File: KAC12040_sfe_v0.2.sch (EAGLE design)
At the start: 9 parts

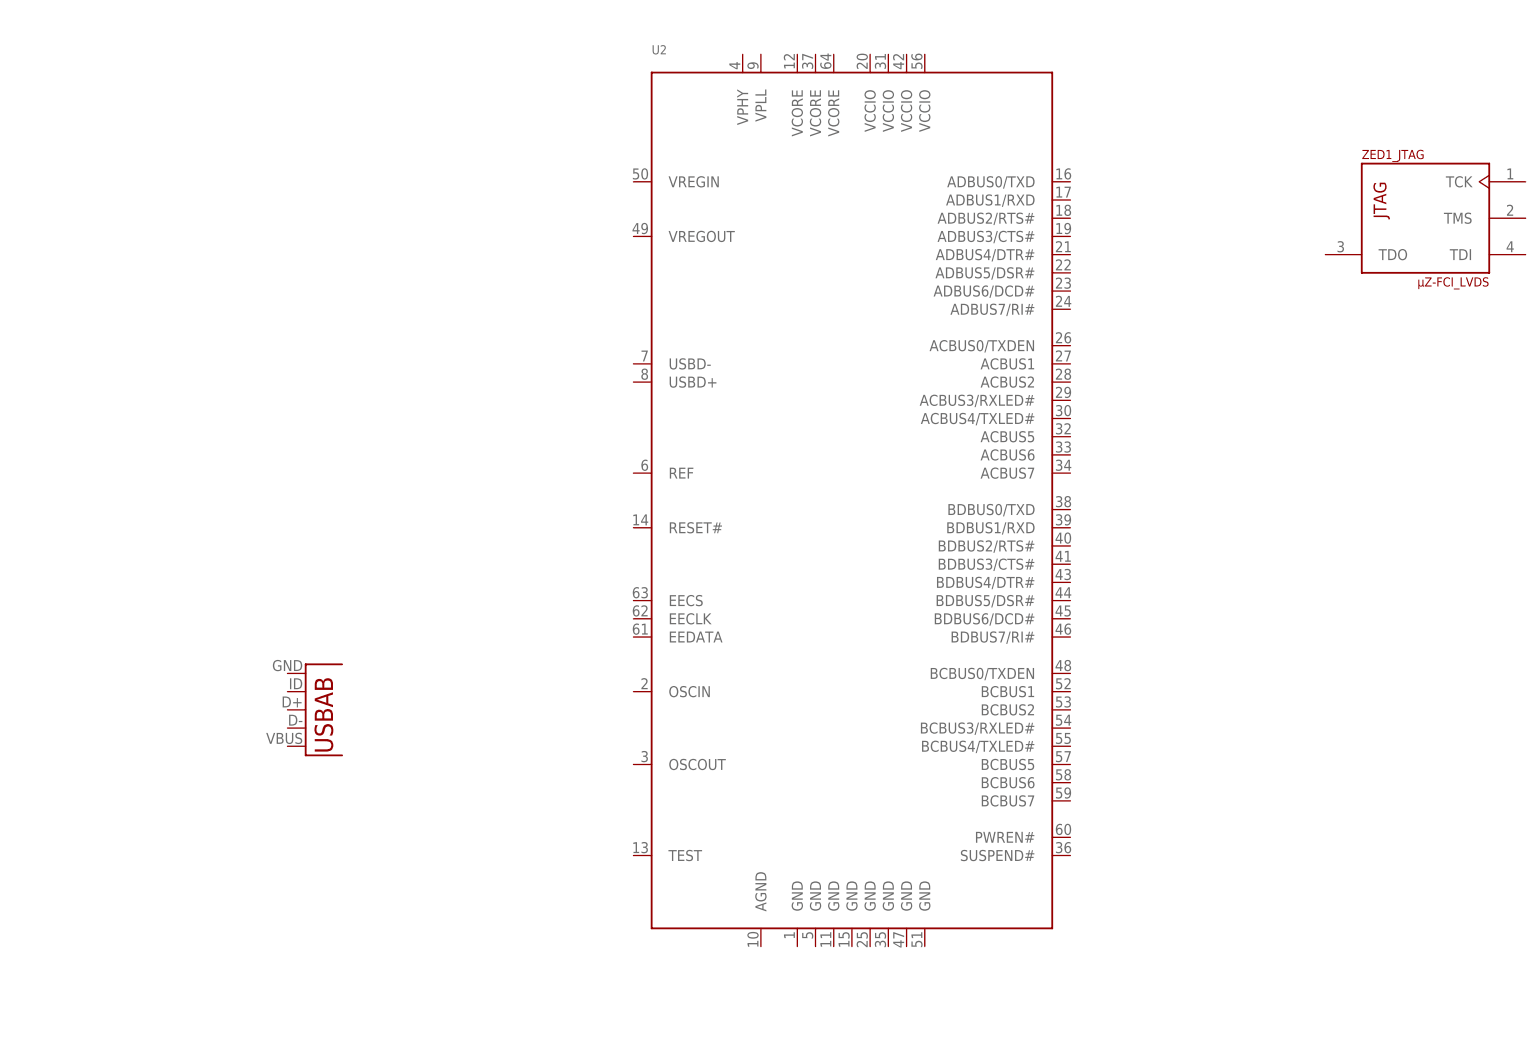
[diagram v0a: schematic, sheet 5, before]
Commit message: Minor library changes and part placement
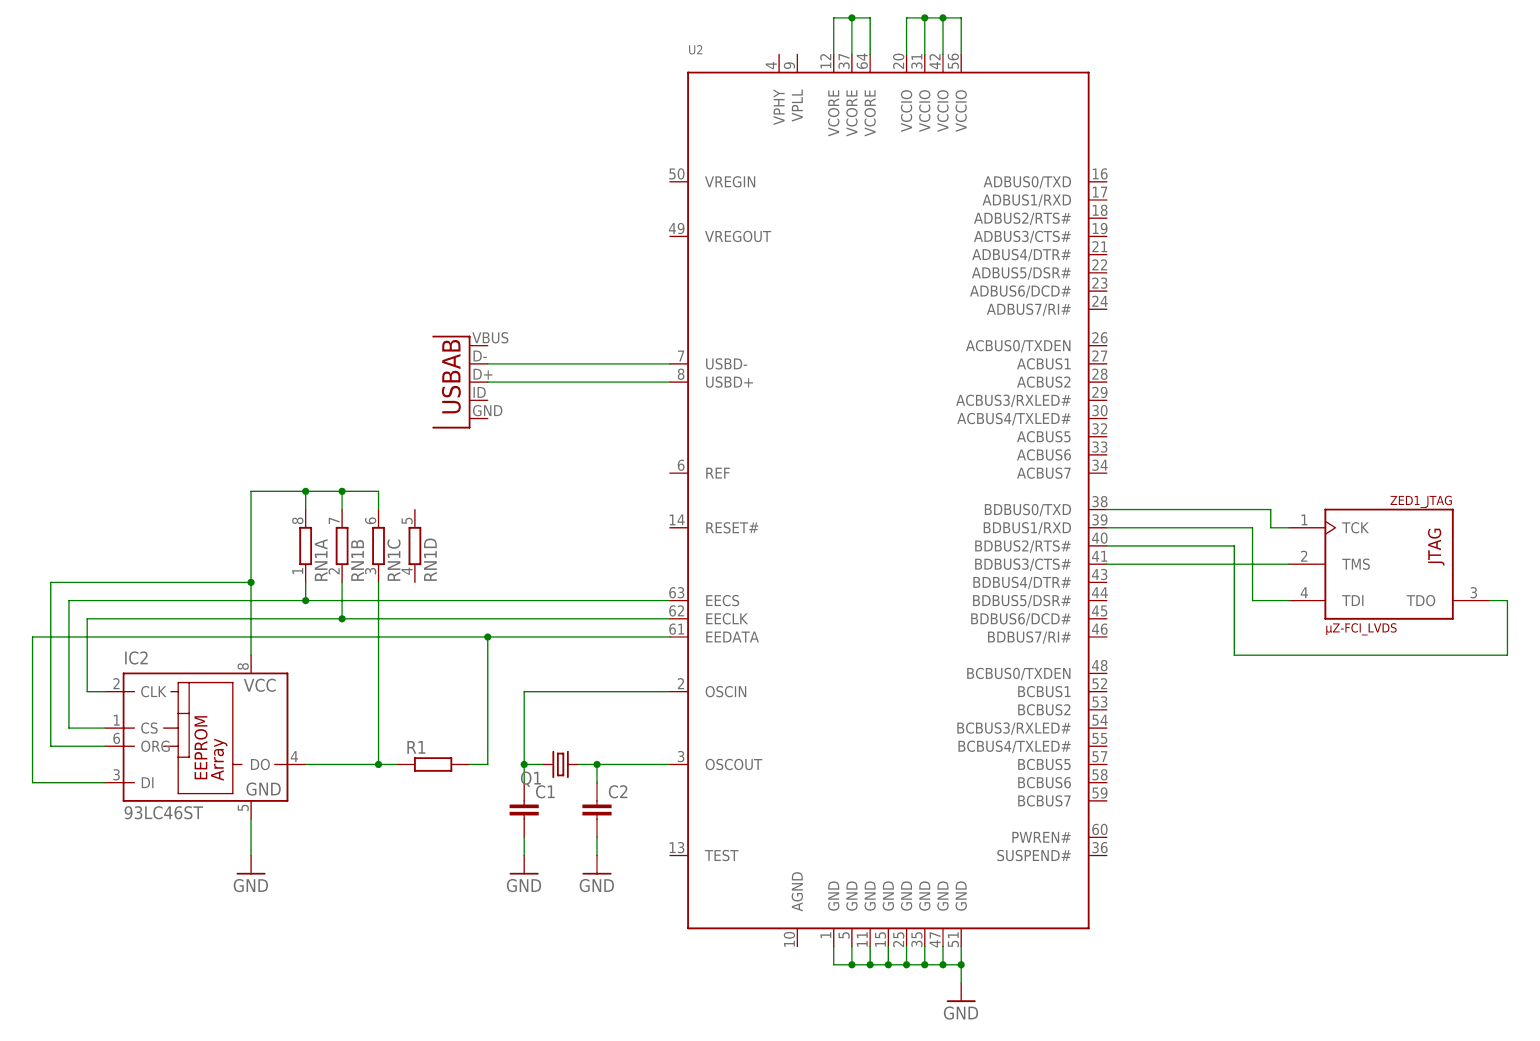
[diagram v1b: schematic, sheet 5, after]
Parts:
- removed U$2: MICRO-SD3, micro-sd:MICRO-SD3
- added C1, C2: (no value), rcl:C-EUC0402K
- added IC2: 93LC46ST, microchip:93LC46ST
- added Q1: (no value), crystal:CRYSTALCTS406
- added R1: (no value), rcl:R-EU_R0402
- added RN1: (no value), resistor-dil:4R-N0402ARV341
- added U$5: ADV7513, adv7513:ADV7513
- added µSD0: MICRO-SD3, micro-sd:MICRO-SD3
- U$1: value KAC-12040 -> KAC-12040-RB501T4; device KAC-12040:KAC-12040 -> KAC-12040:KAC-12040-RB501T4
- renumbered U$3 to µSD1
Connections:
- new net B0_CLK: U$4.B0_CLK, µSD0.5
- new net B0_CMD: U$4.B0_CMD, µSD0.3
- new net B0_DAT0: U$4.B0_DAT0, µSD0.7
- new net B0_DAT1: U$4.B0_DAT1, µSD0.8
- new net B0_DAT2: U$4.B0_DAT2, µSD0.1
- new net B0_DAT3: U$4.B0_DAT3, µSD0.2
- new net B1_CLK: U$4.B1_CLK, µSD1.5
- new net B1_CMD: U$4.B1_CMD, µSD1.3
- new net B1_DAT0: U$4.B1_DAT0, µSD1.7
- new net B1_DAT1: U$4.B1_DAT1, µSD1.8
- new net B1_DAT2: U$4.B1_DAT2, µSD1.1
- new net B1_DAT3: U$4.B1_DAT3, µSD1.2
- new net EE_CLK: IC2.CLK, RN1B.1, U2.EECLK
- new net EE_CS: IC2.CS, RN1A.1, U2.EECS
- new net EE_DATA: IC2.DI, R1.2, U2.EEDATA
- new net GND: C1.2, C2.2, IC2.GND, U2.GND@1, U2.GND@2, U2.GND@3, U2.GND@4, U2.GND@5, U2.GND@6, U2.GND@7, U2.GND@8
- new net N$10: U1.D+, U2.USBD+
- new net N$11: IC2.DO, R1.1, RN1C.1
- new net N$12: IC2.ORG, IC2.VCC, RN1A.2, RN1B.2, RN1C.2
- new net N$13: U2.BDBUS0/TXD, ZED1_JTAG.TCK
- new net N$14: C1.1, Q1.2, U2.OSCIN
- new net N$15: C2.1, Q1.1, U2.OSCOUT
- new net N$16: U2.BDBUS1/RXD, ZED1_JTAG.TDI
- new net N$17: U2.BDBUS2/RTS#, ZED1_JTAG.TDO
- new net N$18: U2.BDBUS3/CTS#, ZED1_JTAG.TMS
- new net N$19: U2.VCCIO@1, U2.VCCIO@2, U2.VCCIO@3, U2.VCCIO@4
- new net N$20: U2.VCORE@1, U2.VCORE@2, U2.VCORE@3
- new net N$21: ZED1JX2_22._P
- new net N$22: ZED1JX2_19._P
- new net N$23: ZED1JX2_03._P
- new net N$24: ZED1JX1_22._P
- new net N$25: ZED1JX1_19._P
- new net N$26: ZED1JX1_03._P
- new net N$5: µSD0.4
- new net N$6: µSD0.6
- new net N$7: µSD1.6
- new net N$8: µSD1.4
- new net N$9: U1.D-, U2.USBD-
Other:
- moved on the sheet: U2, ZED1_JTAG

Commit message: Another update to the design
 - Replaced FT2232H with FT232H (single channel)
 - Added SD PMOD interface
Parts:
- added C3: 100n, rcl:C-EUC0402K
- added FB1: 600R, microbuilder:FERRITE_0603MP
- added R2: 12k, rcl:R-EU_R0402
- added U$2: FT232H, ft232h:FT232H
- R1: value (none) -> 2k
- U2: value (none) -> TPD3E001DRLR; device microbuilder:FT2232H -> esd:TPD3E001DRLR
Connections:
- new net A_CLK: U$4.A_CLK, ZED1_PMOD.PMOD_D3
- new net A_CMD: U$4.A_CMD, ZED1_PMOD.PMOD_D2
- new net A_DAT0: U$4.A_DAT0, ZED1_PMOD.PMOD_D1
- new net A_DAT1: U$4.A_DAT1, ZED1_PMOD.PMOD_D0
- new net A_DAT2: U$4.A_DAT2, ZED1_PMOD.PMOD_D6
- new net A_DAT3: U$4.A_DAT3, ZED1_PMOD.PMOD_D7
- new net N$27: RN1D.1, U$2.RESET#
- new net N$28: U$2.DP, U1.D+, U2.IO2
- new net N$29: U$2.DM, U1.D-, U2.IO1
- new net N$30: U$4.GND@11, U$4.GND@2
- new net N$32: R2.2, U$2.REF
- new net SEL: U$4.SEL, ZED1_PMOD.PMOD_D4
- net EE_CLK: now also U$2.EECLK; no longer U2.EECLK
- net EE_CS: now also U$2.EECS; no longer U2.EECS
- net EE_DATA: now also U$2.EEDATA; no longer U2.EEDATA
- net GND: now also C3.2, R2.1, U$2.AGND@4, U$2.AGND@41, U$2.AGND@9, U$2.GND@10, U$2.GND@11, U$2.GND@22, U$2.GND@23, U$2.GND@35, U$2.GND@36, U$2.GND@47, U$2.GND@48, U1.GND, U2.GND; no longer U2.GND@1, U2.GND@2, U2.GND@3, U2.GND@4, U2.GND@5, U2.GND@6, U2.GND@7, U2.GND@8
- net N$10: now also C3.1, FB1.P$1, U1.VBUS, U2.VCC; no longer U1.D+, U2.USBD+
- net N$13: now also U$2.ADBUS0; no longer U2.BDBUS0/TXD
- net N$14: now also U$2.OSCI; no longer U2.OSCIN
- net N$15: now also U$2.OSCO; no longer U2.OSCOUT
- net N$16: now also U$2.ADBUS1; no longer U2.BDBUS1/RXD
- net N$17: now also U$2.ADBUS2; no longer U2.BDBUS2/RTS#
- net N$18: now also U$2.ADBUS3; no longer U2.BDBUS3/CTS#
- net N$19: now also U$2.VCCIO@12, U$2.VCCIO@24, U$2.VCCIO@46; no longer U2.VCCIO@1, U2.VCCIO@2, U2.VCCIO@3, U2.VCCIO@4
- net N$20: now also U1.USBID, U2.IO3; no longer U2.VCORE@1, U2.VCORE@2, U2.VCORE@3
- net N$9: now also FB1.P$2, U$2.VREGIN; no longer U1.D-, U2.USBD-
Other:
- moved on the sheet: C1, C2, IC2, Q1, R1, RN1A, RN1B, RN1C, RN1D, ZED1_JTAG, ZED1_PMOD
